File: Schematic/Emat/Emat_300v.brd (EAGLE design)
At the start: 100 x 80 mm, 45 parts, among them IC1 UC3843N, Q1 BSS138, Q2 IRF640IW220B

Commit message: Further work on schematic.
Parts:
- added C14: 1.2nF 630V K78-2, rcl:C150-064X183
- added C15: 220pF 1000V, rcl:C075-042X103
- added C16, C17: 330nF 630V K73-17, rcl:C225-062X268
- added C19: 47uF 450V, rcl:E7,5-18
- added D7: MUR4100, diode:DO201-15
- added J1, J2: PIN1-2, con-faston:62221
- added R21, R22: 100, resistor:R2512
- added R23, R24: 51, resistor:R1206
- added T1: EFD25-2, trafo:EFD25
- R5: value 4.7K -> 3.6K
- moved C1 130.1 mm to (73.7, 74.9)
- moved R1 111.9 mm to (73.7, 66.0)
- moved OK1 104.4 mm to (57.1, 68.6), turned to 90 degrees
- moved D1 97.1 mm to (81.3, 61.0), turned to 270 degrees
- moved D2 86.7 mm to (81.3, 35.6), turned to 270 degrees
- moved Q1 67.4 mm to (78.7, 74.9)
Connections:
- removed net N$2: R1.2
- new net N$18: J1.1, OK2.1
- new net N$19: J2.1, OK2.2
- new net N$20: Q2.D, R21.2, R22.2, T1.1
- new net N$21: C14.1, R21.1, R22.1
- new net N$22: C15.2, D7.A, T1.7
- new net N$24: R23.1, R24.2
- new net N$25: C15.1, R23.2
- new net V+: C16.1, C17.1, C19.+, D1.C, D7.C, R1.2, R24.1
- new net V-: C16.2, C17.2, C19.-, D2.A, T1.12
- net +12V: now also T1.6
- net GND: now also C14.2

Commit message: 300V pcb done
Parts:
- removed C17: 330nF 630V K73-17, rcl:C225-062X268
- added J3, J4, J5, J6: PIN1-2, con-faston:62221
- added R25, R26: 220K, resistor:R1206
- moved J1 414.4 mm to (33.7, 72.4), turned to 180 degrees
- moved J2 406.2 mm to (33.7, 62.2), turned to 180 degrees
- moved R22 387.7 mm to (63.5, 16.5), turned to 90 degrees
- moved C14 383.8 mm to (49.5, 8.89), flipped to the bottom
- moved R21 380.3 mm to (59.1, 16.5), turned to 90 degrees
- moved C13 353.0 mm to (24.1, 10.2), turned to 90 degrees
- moved C12 348.2 mm to (46.4, 8.26), turned to 180 degrees
- moved C9 347.9 mm to (28.6, 23.5), turned to 90 degrees
- moved C11 347.2 mm to (27.9, 16.5), turned to 180 degrees
- moved C10 334.7 mm to (31.8, 23.5), flipped to the bottom, turned to 90 degrees
- moved OK2 313.6 mm to (23.5, 67.3), flipped to the bottom, turned to 270 degrees
- moved R20 306.2 mm to (12.7, 40.6)
- moved C7 296.9 mm to (38.1, 44.5), turned to 90 degrees
- moved L2 294.2 mm to (30.5, 6.35), flipped to the bottom, turned to 180 degrees
- moved R19 291.5 mm to (12.7, 48.3), turned to 90 degrees
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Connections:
- new net N$2: R25.1, R26.2
- net GND: now also J6.1
- net N$16: now also J5.1
- net V+: now also J3.1, R25.2; no longer C17.1
- net V-: now also J4.1, R26.1; no longer C17.2
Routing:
- net GND: track 0.00 -> 237.5 mm, vias 0 -> 5
- net +12V: track 0.00 -> 153.1 mm
- net V+: track 0.00 -> 108.1 mm
- net N$14: track 0.00 -> 92.0 mm, vias 0 -> 2
- net V-: track 0.00 -> 76.9 mm
- net N$5: track 0.00 -> 68.0 mm, vias 0 -> 2
- net N$13: track 0.00 -> 64.7 mm
- net VCC: track 0.00 -> 63.9 mm
- net N$15: track 0.00 -> 42.0 mm
- net N$17: track 0.00 -> 36.7 mm
- net N$11: track 0.00 -> 34.4 mm
- net N$1: track 0.00 -> 23.0 mm
- net N$20: track 0.00 -> 18.5 mm
- net N$16: track 0.00 -> 14.7 mm
- net N$10: track 0.00 -> 12.9 mm
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
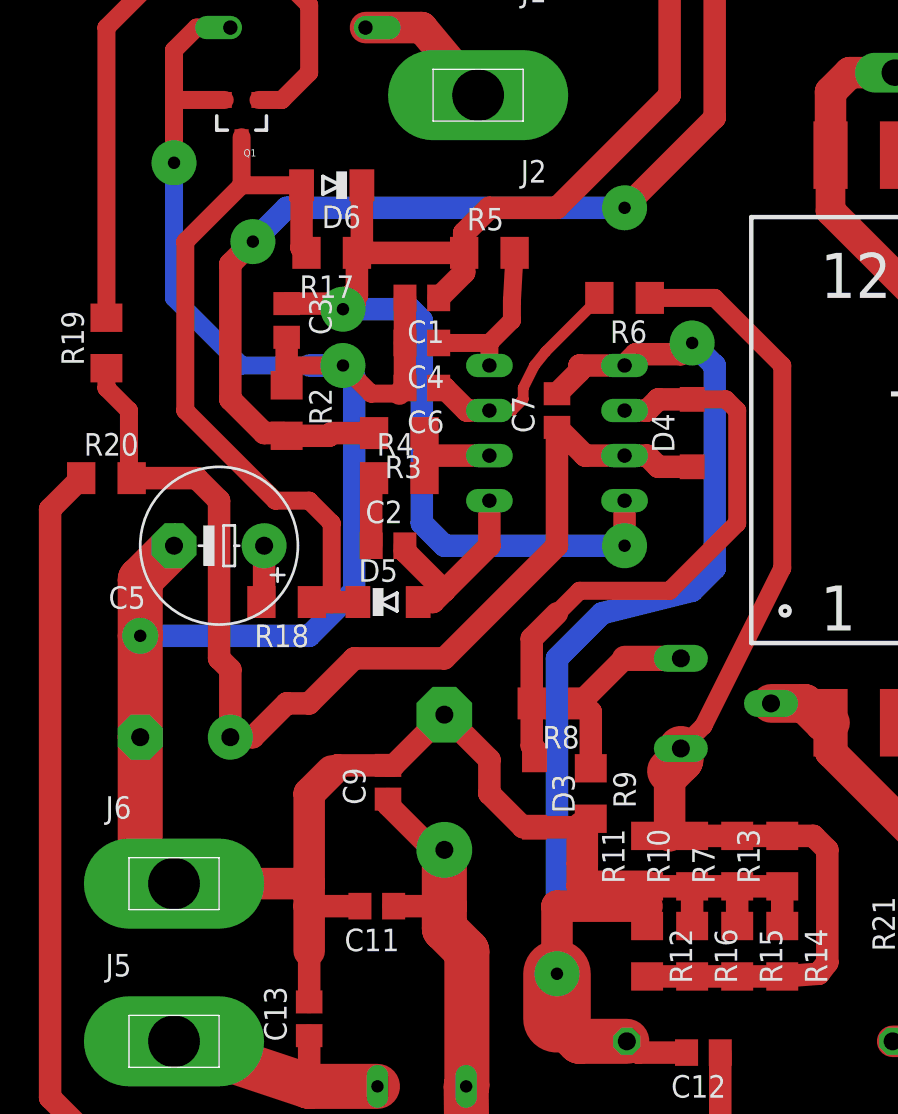
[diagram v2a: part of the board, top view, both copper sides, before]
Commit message: 300V PCB modified, BOM added.
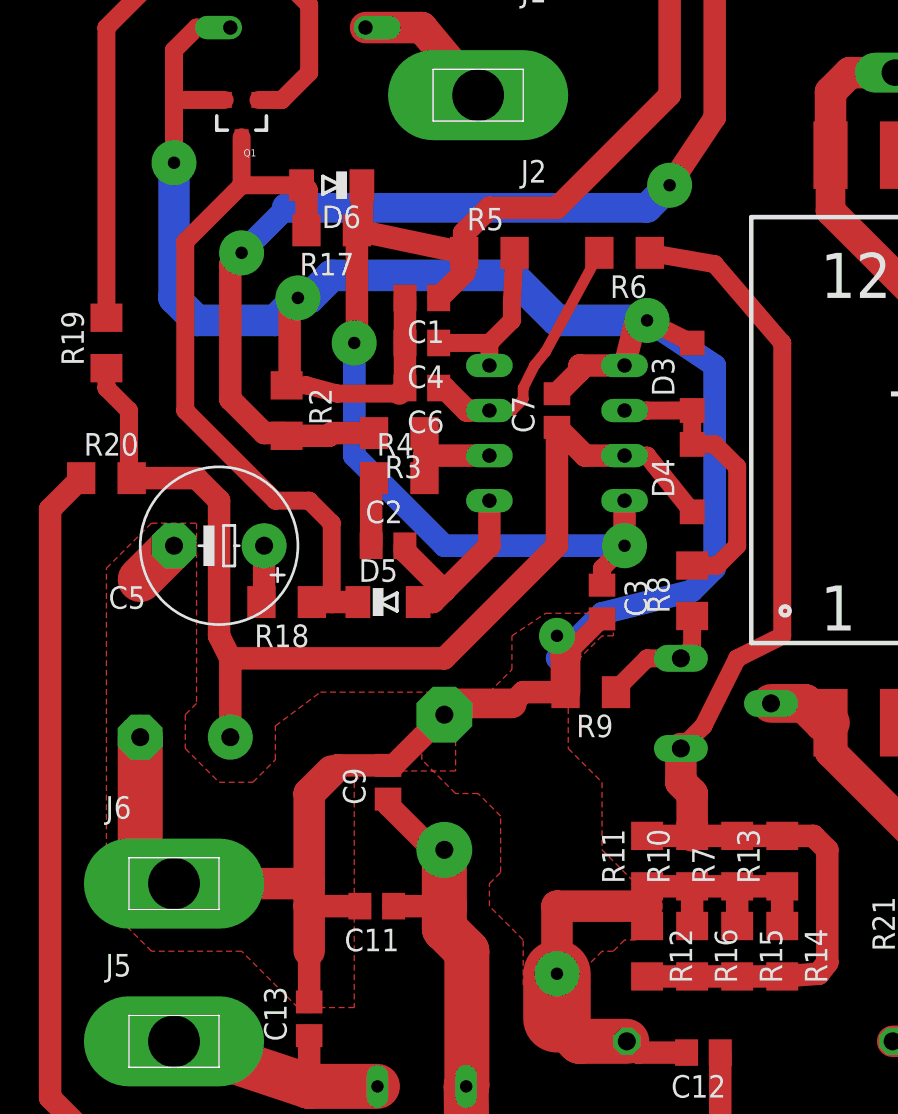
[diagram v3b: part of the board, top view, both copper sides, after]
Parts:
- moved D3 25.1 mm to (45.7, 46.4), turned to 90 degrees
- moved C3 23.8 mm to (40.6, 33.7)
- moved R8 9.92 mm to (45.7, 34.3), turned to 90 degrees
- moved R9 5.71 mm to (40.0, 28.6), turned to 180 degrees
- moved R6 2.54 mm to (41.9, 53.3)
- moved D4 2.54 mm to (45.7, 40.6)
- moved R17 1.27 mm to (25.4, 54.6)
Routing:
- net GND: track 237.5 -> 202.6 mm
- net N$11: track 34.4 -> 16.2 mm
- net N$14: track 92.0 -> 87.4 mm
- net N$12: track 10.6 -> 7.19 mm
- net N$13: track 64.7 -> 67.5 mm
- net N$10: track 12.9 -> 15.0 mm
- net N$15: track 42.0 -> 40.7 mm
- net VCC: track 63.9 -> 63.2 mm
- added copper zone on layer 1, net GND

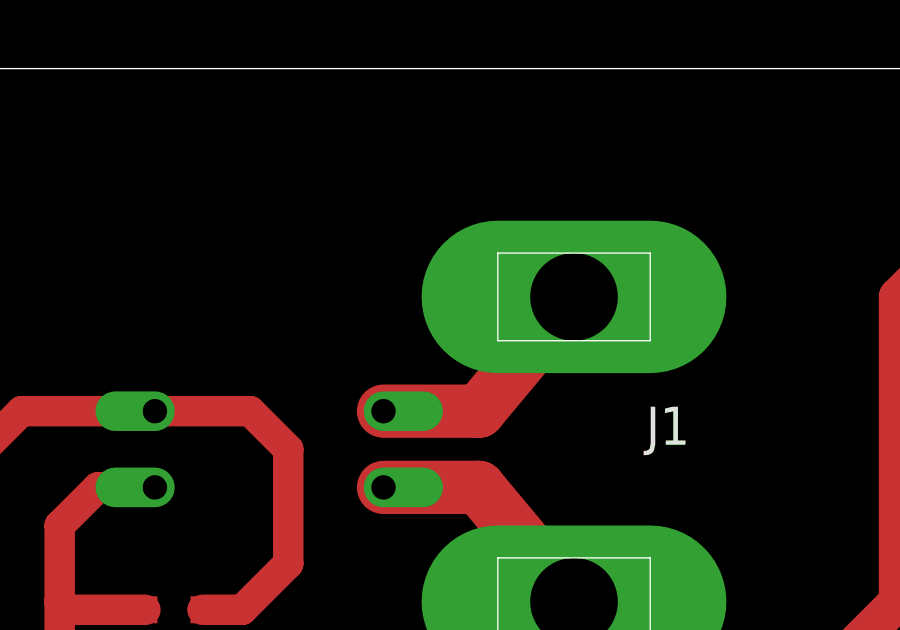
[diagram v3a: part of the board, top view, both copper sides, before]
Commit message: Add resistor before opto-coupler.
To enable direct controll from STM32.
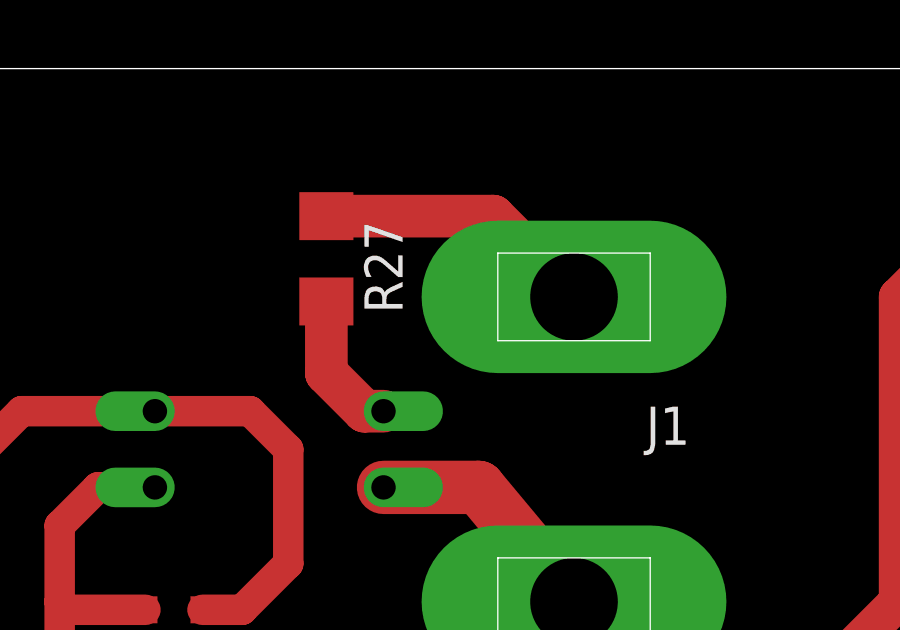
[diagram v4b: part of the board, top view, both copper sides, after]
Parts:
- added R27: 1K, resistor:R1206
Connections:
- new net N$23: J1.1, R27.1
- net N$18: now also R27.2; no longer J1.1
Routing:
- net N$23: track 0.00 -> 9.37 mm
- net N$18: track 8.13 -> 4.82 mm
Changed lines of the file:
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@@
 <element name="R25" library="resistor" package="R1206" value="220K" x="81.915" y="45.72"/>
 <element name="R26" library="resistor" package="R1206" value="220K" x="75.565" y="45.72"/>
+<element name="R27" library="resistor" package="R1206" value="1K" x="25.4" y="73.66" rot="R270"/>
 </elements>
 <signals>
@@
 <wire x1="24.13" y1="9.21" x2="24.13" y2="6.35" width="1.27" layer="1"/>
 </signal>
-<signal name="N$18">
-<contactref element="OK2" pad="1"/>
-<contactref element="J1" pad="1"/>
-<wire x1="27.305" y1="68.58" x2="30.48" y2="68.58" width="1.778" layer="1"/>
-<wire x1="30.48" y1="68.58" x2="33.655" y2="72.39" width="1.778" layer="1"/>
-</signal>
 <signal name="N$19">
 <contactref element="OK2" pad="2"/>
@@
 <wire x1="76.987" y1="45.72" x2="80.493" y2="45.72" width="1.27" layer="1"/>
 </signal>
+<signal name="N$18">
+<contactref element="OK2" pad="1"/>
+<contactref element="R27" pad="2"/>
+<wire x1="27.305" y1="68.58" x2="26.67" y2="68.58" width="1.4224" layer="1"/>
+<wire x1="26.67" y1="68.58" x2="25.4" y2="69.85" width="1.4224" layer="1"/>
+<wire x1="25.4" y1="69.85" x2="25.4" y2="72.238" width="1.4224" layer="1"/>
+</signal>
+<signal name="N$23">
+<contactref element="R27" pad="1"/>
+<contactref element="J1" pad="1"/>
+<wire x1="25.4" y1="75.082" x2="30.963" y2="75.082" width="1.4224" layer="1"/>
+<wire x1="30.963" y1="75.082" x2="33.655" y2="72.39" width="1.4224" layer="1"/>
+</signal>
 </signals>

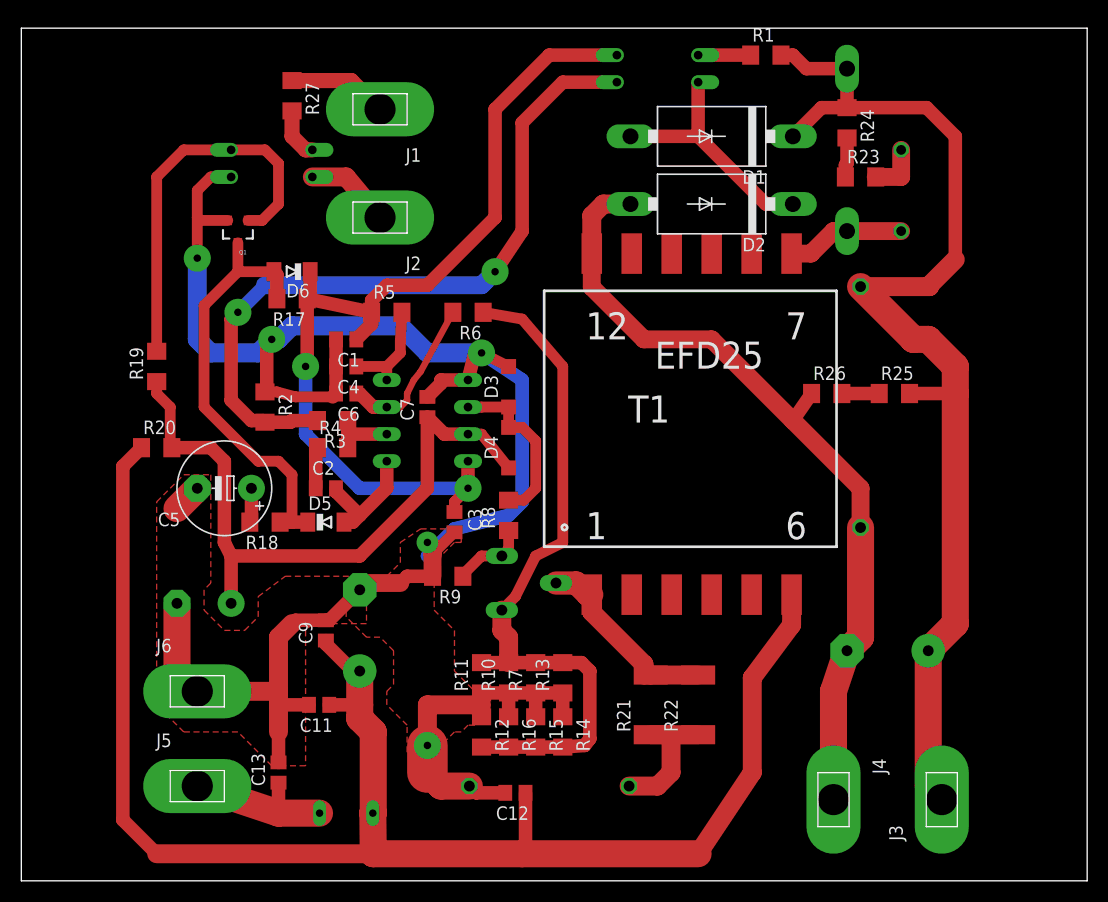
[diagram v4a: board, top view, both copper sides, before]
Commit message: Modify board to fit to pcb.
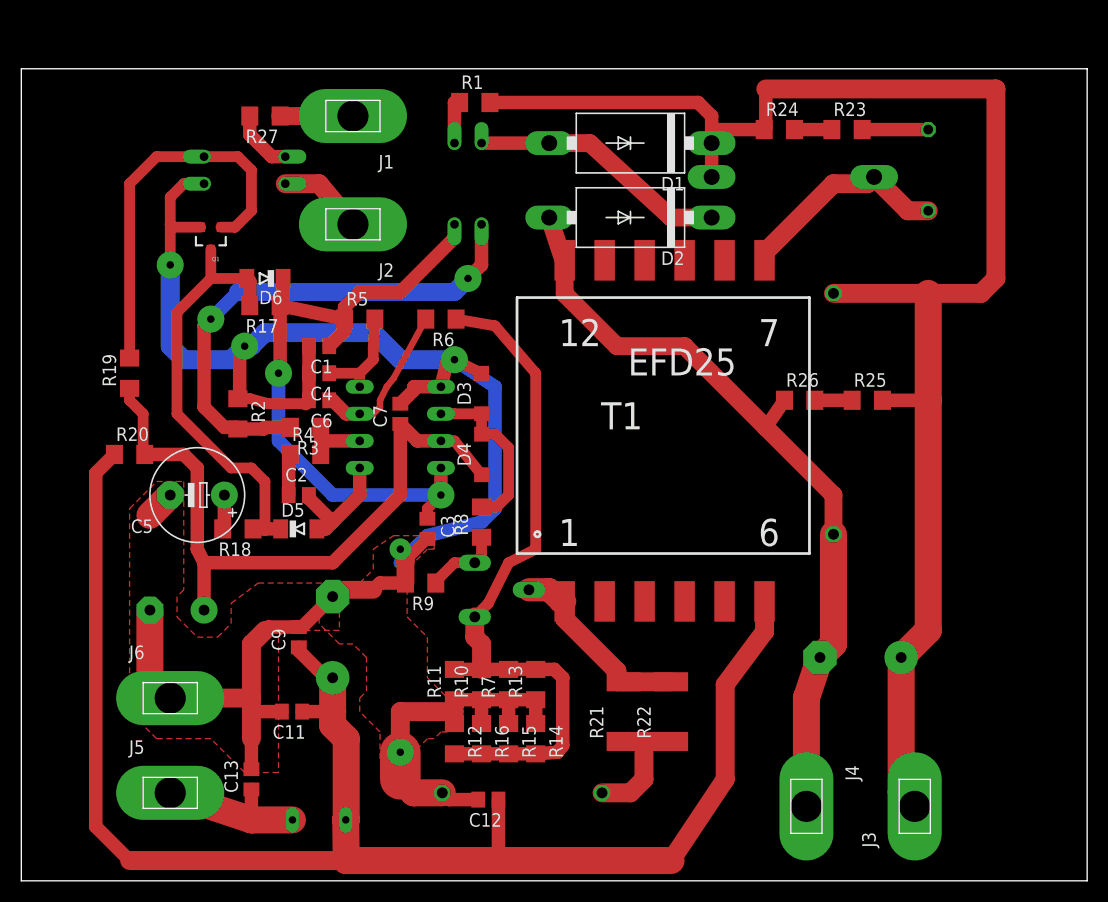
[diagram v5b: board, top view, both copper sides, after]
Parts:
- moved R1 27.7 mm to (42.5, 73.0)
- moved OK1 20.8 mm to (41.9, 65.4), turned to 180 degrees
- moved D2 7.73 mm to (57.1, 62.2)
- moved D1 7.65 mm to (57.1, 69.2)
- moved R24 6.38 mm to (71.1, 70.5), turned to 0 degrees
- moved D7 5.68 mm to (72.4, 66.0), turned to 180 degrees
- moved R23 4.62 mm to (77.5, 70.5)
- moved C15 3.18 mm to (85.1, 66.7)
- moved R27 3.18 mm to (22.9, 71.8), turned to 180 degrees
- moved C19 2.62 mm to (78.7, 21.0)
- moved J3 2.62 mm to (83.8, 6.99)
- moved J4 2.62 mm to (73.7, 6.99)
- moved R25 2.62 mm to (79.4, 45.1)
- moved J1 2.62 mm to (31.1, 71.8)
- moved OK2 2.62 mm to (21.0, 66.7)
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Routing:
- net V+: track 108.1 -> 145.0 mm
- net N$14: track 87.4 -> 63.2 mm
- net N$5: track 68.5 -> 48.9 mm
- net N$22: track 11.2 -> 20.3 mm
- net V-: track 76.9 -> 73.5 mm
- net N$23: track 9.37 -> 6.83 mm
- net N$1: track 23.0 -> 24.3 mm
- net N$25: track 4.93 -> 6.20 mm
- net N$18: track 4.82 -> 5.93 mm
- net N$3: track 4.93 -> 4.29 mm
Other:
- board size 100 x 80 mm -> 100 x 76.2 mm

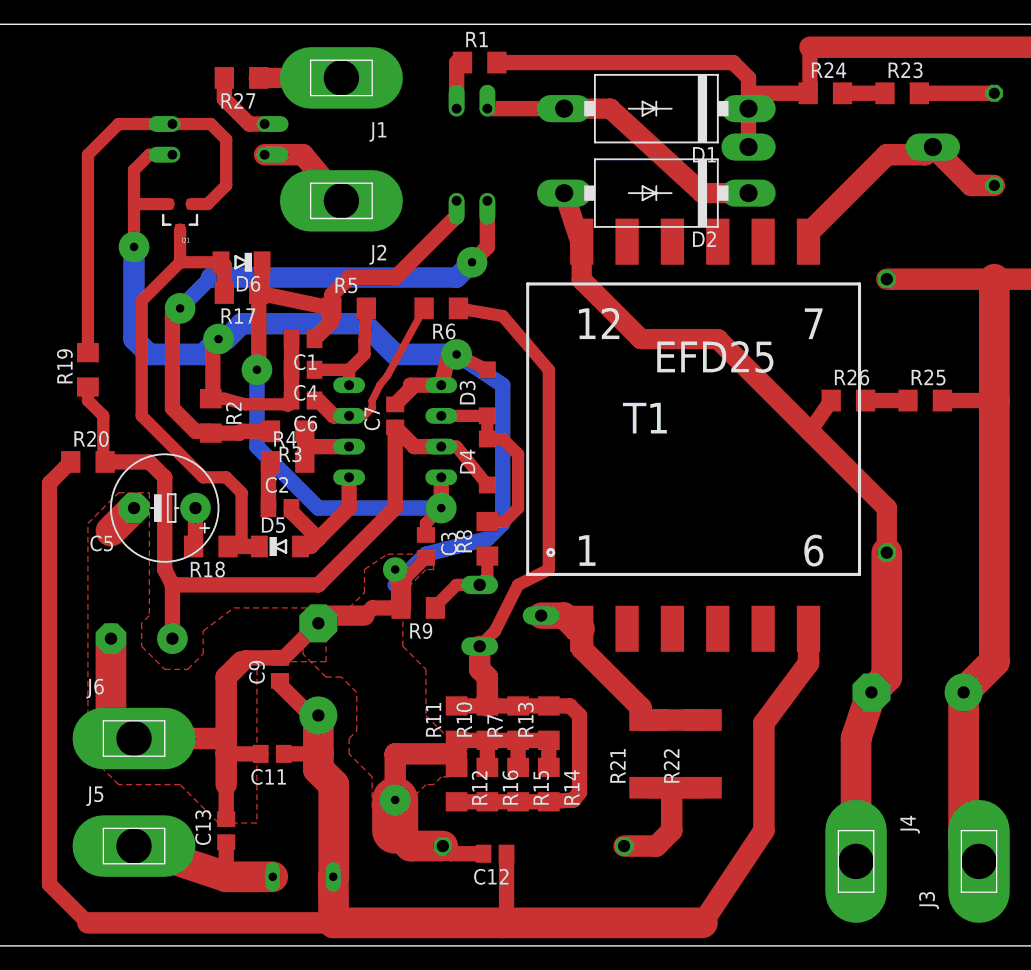
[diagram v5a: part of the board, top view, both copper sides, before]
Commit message: Add HV On Off command.
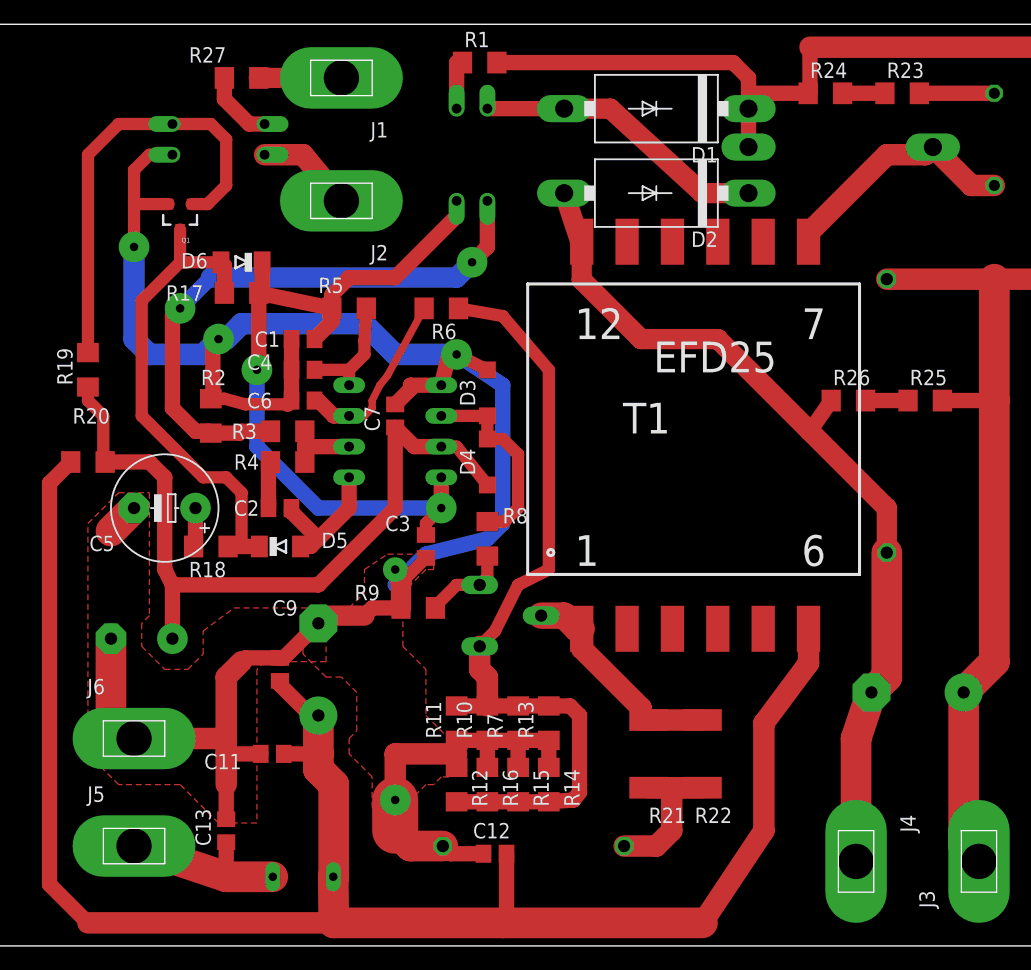
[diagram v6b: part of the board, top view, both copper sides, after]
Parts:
- R27: value 1K -> 510
